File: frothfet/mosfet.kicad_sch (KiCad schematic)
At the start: 25 parts, among them Q1 AO3400A, Q2 BSC010N04LS, U1 SN74LVC1G14DBV, U2 LM74502H, U3 TMCS1108A2U

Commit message: bom and placement all check out.  ready for production!
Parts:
- Q2, U3: Rotation Offset (none) -> -90
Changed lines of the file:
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@@
+			)
+		)
+		(property "Rotation Offset" "-90"
+			(at 156.21 107.95 0)
+			(effects
+				(font
+					(size 1.27 1.27)
+				)
+				(hide yes)
 			)
 		)
@@
 			(at 143.51 58.42 0)
 			(effects
+				(font
+					(size 1.27 1.27)
+				)
+				(hide yes)
+			)
+		)
+		(property "Rotation Offset" "-90"
+			(at 143.51 58.42 0)
+			(effects

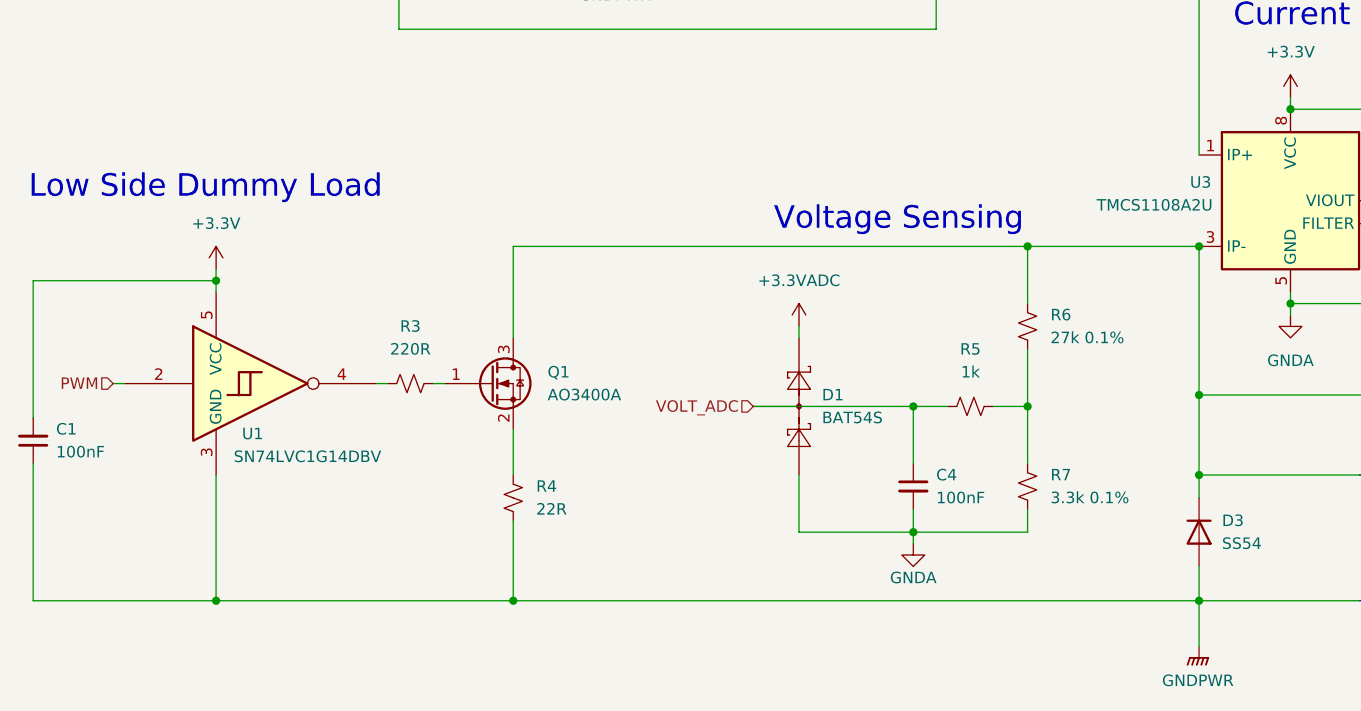
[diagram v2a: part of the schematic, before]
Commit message: removed unneccesary bleed circuit
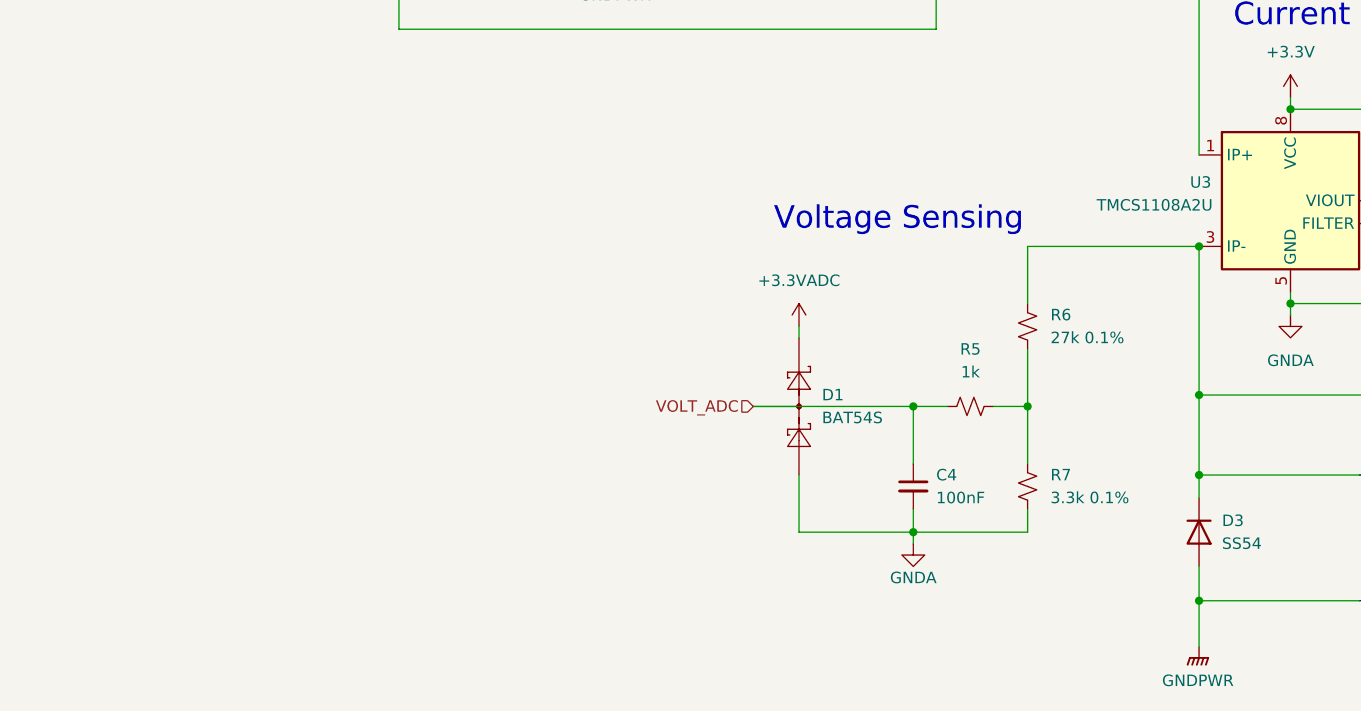
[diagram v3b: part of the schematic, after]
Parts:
- removed C1: 100nF, Capacitor_SMD:C_0603_1608Metric, symbol Device:C_Small
- removed Q1: AO3400A, Package_TO_SOT_SMD:SOT-23, symbol Transistor_FET:AO3400A
- removed R3: 220R, Resistor_SMD:R_0603_1608Metric, symbol Device:R_Small_US
- removed R4: 22R, Resistor_SMD:R_1206_3216Metric, symbol Device:R_Small_US
- removed U1: SN74LVC1G14DBV, Package_TO_SOT_SMD:SOT-23-5, symbol 74xGxx:SN74LVC1G14DBV
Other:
- note removed: "Low Side Dummy Load"

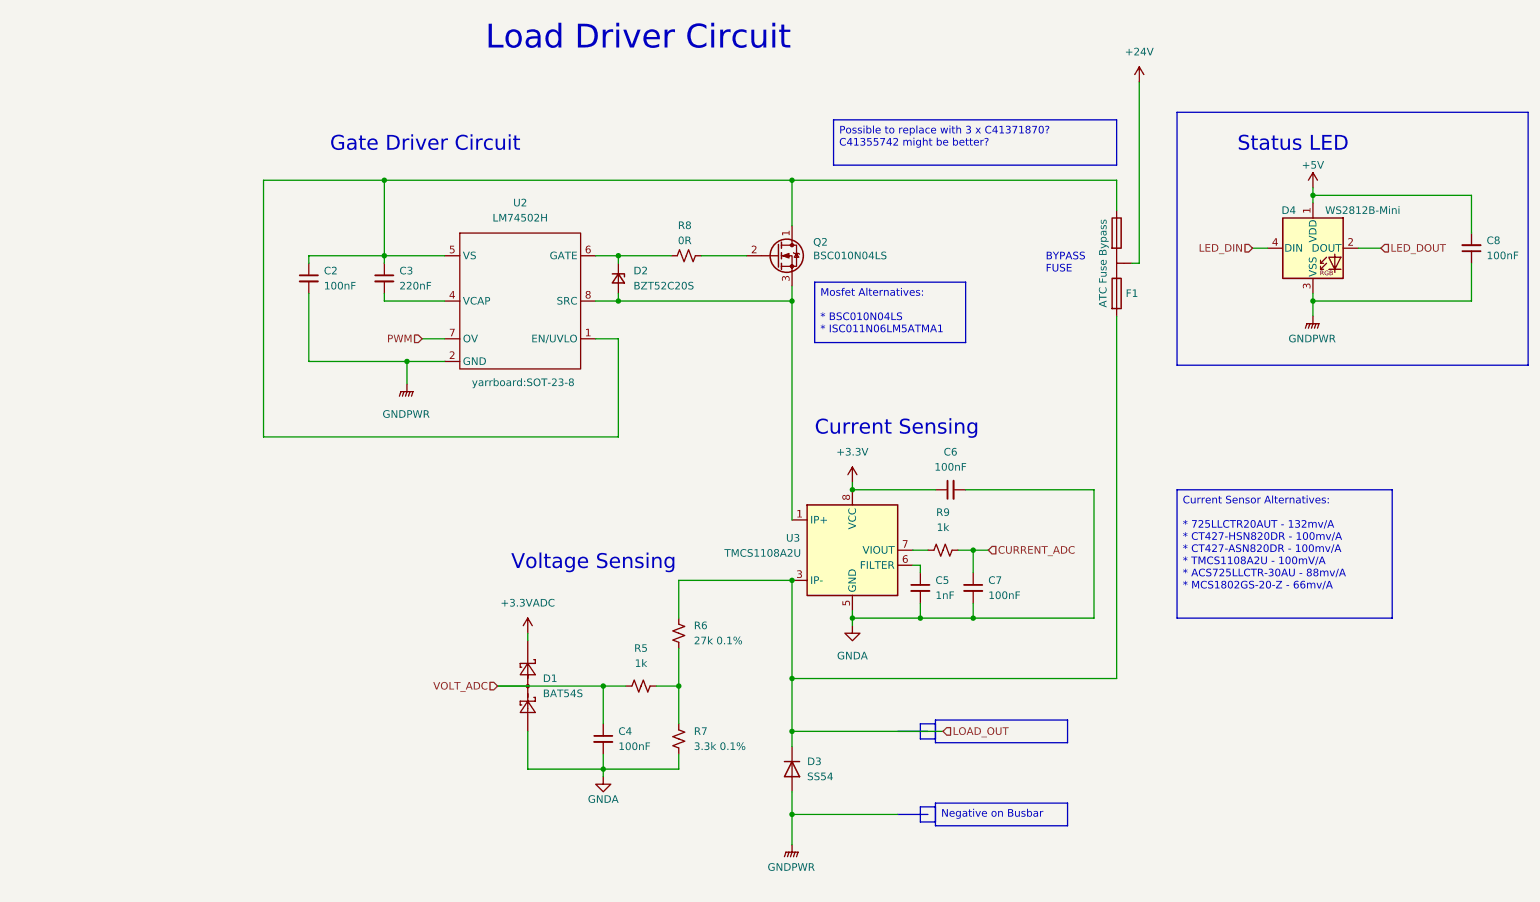
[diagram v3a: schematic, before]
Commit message: switched to ina226 for voltage and current measurement
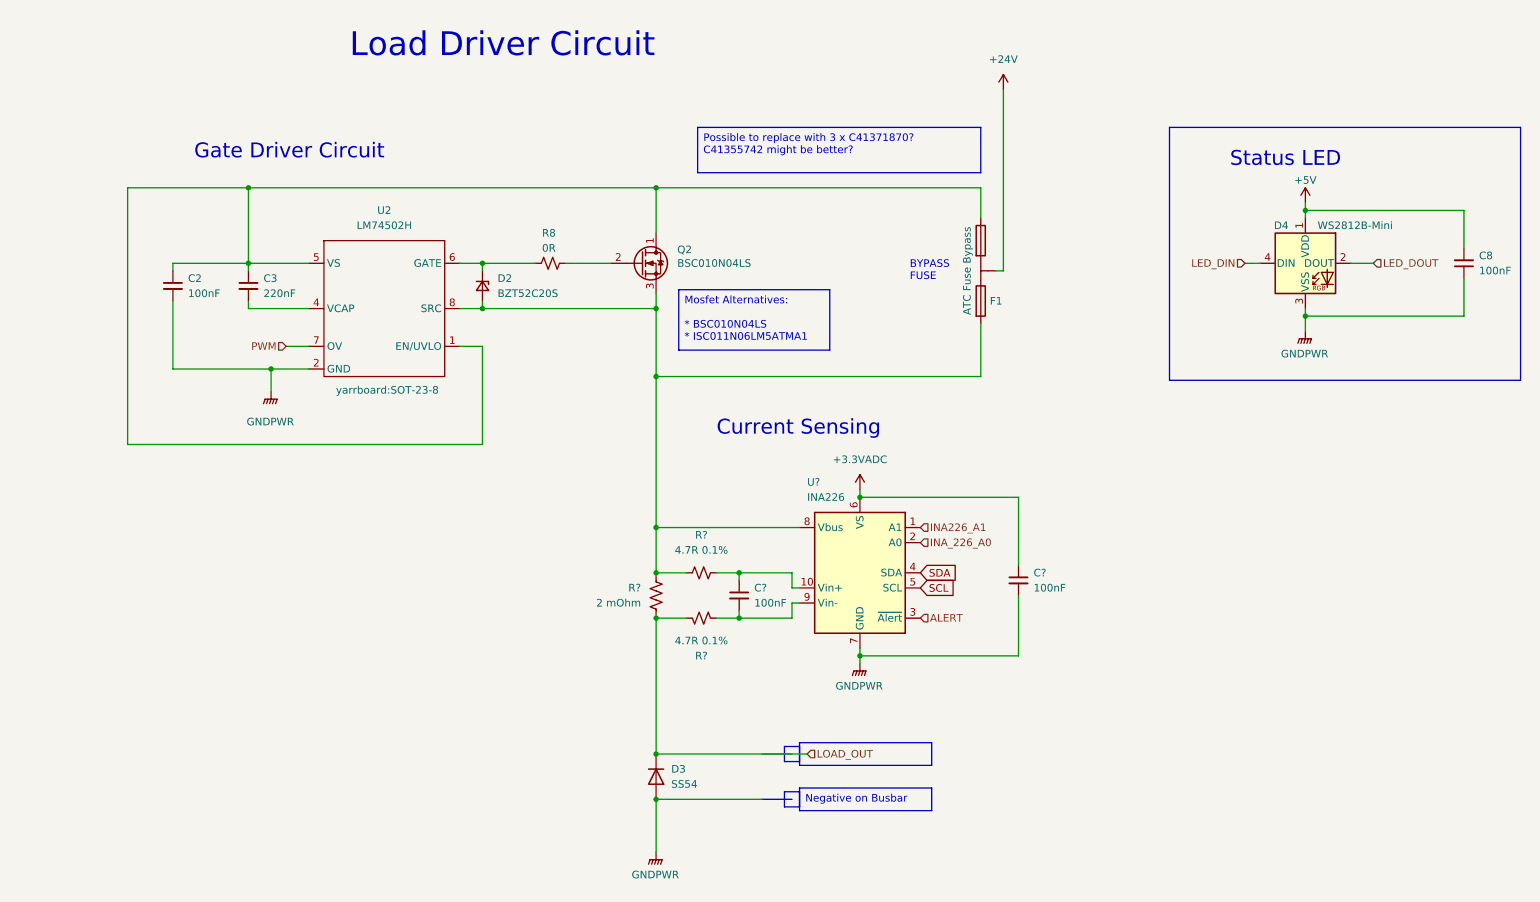
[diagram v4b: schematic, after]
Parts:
- removed C4, C6, C7: 100nF, Capacitor_SMD:C_0603_1608Metric, symbol Device:C_Small
- removed C5: 1nF, Capacitor_SMD:C_0603_1608Metric, symbol Device:C_Small
- removed D1: BAT54S, Package_TO_SOT_SMD:SOT-23, symbol Diode:BAT54S
- removed R5, R9: 1k, Resistor_SMD:R_0603_1608Metric, symbol Device:R_Small_US
- removed R6: 27k 0.1%, Resistor_SMD:R_0603_1608Metric, symbol Device:R_Small_US
- removed R7: 3.3k 0.1%, Resistor_SMD:R_0603_1608Metric, symbol Device:R_Small_US
- removed U3: TMCS1108A2U, yarrboard:ACS7XX, symbol Sensor_Current:ACS725xLCTR-20AU
- added C? (x2): 100nF, Capacitor_SMD:C_0603_1608Metric, symbol Device:C_Small
- added R?: 2 mOhm, Resistor_SMD:R_4020_10251Metric, symbol Device:R_US
- added R? (x2): 4.7R 0.1%, Resistor_SMD:R_0603_1608Metric, symbol Device:R_Small_US
- added U?: INA226, Package_SO:VSSOP-10_3x3mm_P0.5mm, symbol Sensor_Energy:INA226
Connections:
- net +3.3VADC: now also C?.1, U?.6 (VS)
- net GNDPWR: now also C?.2, U?.7 (GND)
- net LOAD_OUT: now also R?.2, R?.2; no longer F1.3
- net at D2.2 (A), Q2.3 (S), U2.8 (SRC): now also F1.3, R?.1, R?.2, U?.8 (Vbus)
- new net: C?.1, R?.1, U?.10 (Vin+)
- new net: C?.2, R?.1, U?.9 (Vin-)
- new net ALERT: U?.3 (~{Alert})
- new net INA226_A1: U?.1 (A1)
- new net INA_226_A0: U?.2 (A0)
- new net SCL: U?.5 (SCL)
- new net SDA: U?.4 (SDA)
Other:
- note removed: "Voltage Sensing"
- moved on the sheet: C2, C3, C8, D2, D3, D4, F1, Q2, R8, U2

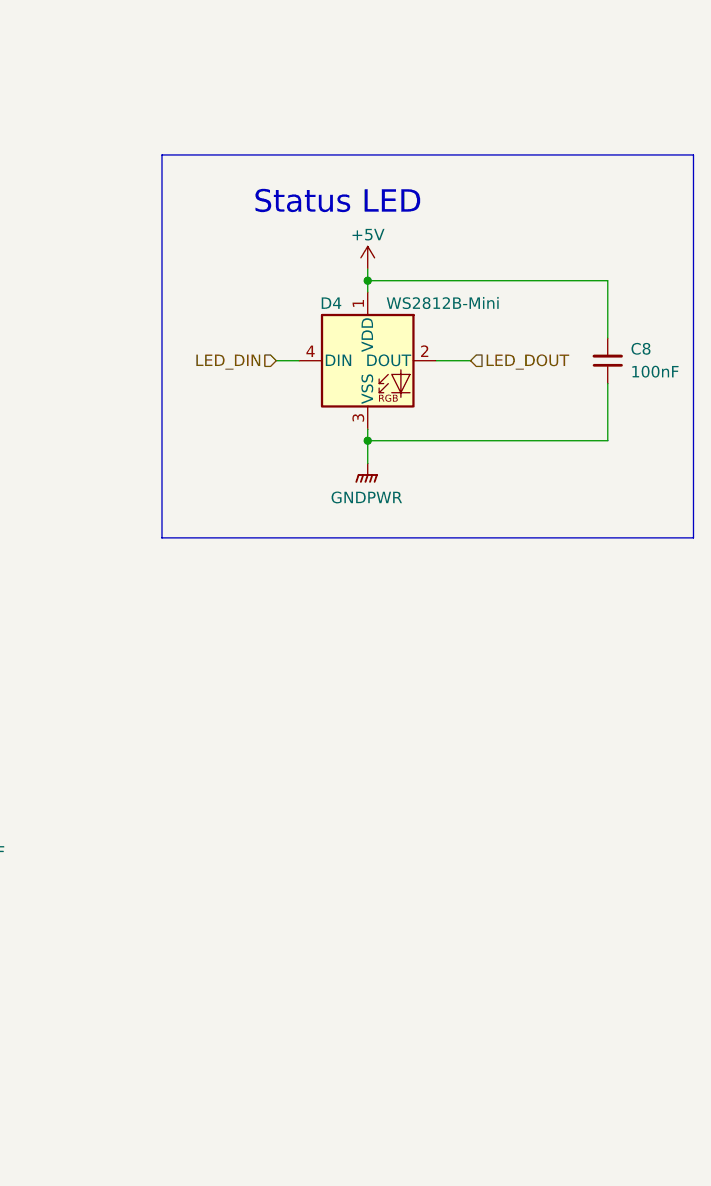
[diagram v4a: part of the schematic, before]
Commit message: added lm75b temperature sensor to channels.
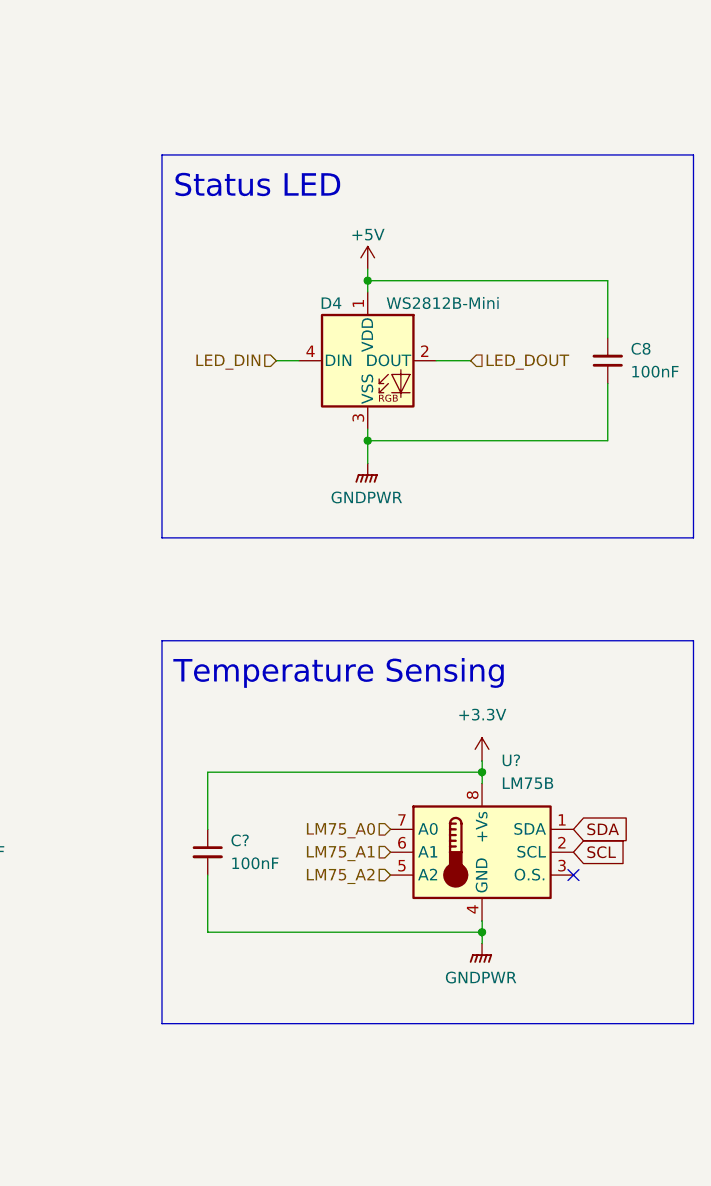
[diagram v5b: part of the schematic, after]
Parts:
- added C?: 100nF, Capacitor_SMD:C_0603_1608Metric, symbol Device:C_Small
- added U?: LM75B, symbol Sensor_Temperature:LM75B
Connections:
- net GNDPWR: now also C?.2, U?.4 (GND)
- net SCL: now also U?.2 (SCL)
- net SDA: now also U?.1 (SDA)
- new net +3.3V: C?.1, U?.8 (+Vs)
- new net LM75_A0: U?.7 (A0)
- new net LM75_A1: U?.6 (A1)
- new net LM75_A2: U?.5 (A2)
- no-connect marks 0 -> 1
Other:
- note added: "Temperature Sensing"

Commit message: wired the i2c addresses.
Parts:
- U3: renamed from U?; footprint (none) -> Package_SO:SOIC-8_3.9x4.9mm_P1.27mm; LCSC (none) -> C34565
- gave numbers to parts that had none: 7
- renumbered C2 to C1, C3 to C2, C8 to C6, D2 to D1, D3 to D2, D4 to D3, Q2 to Q1, R8 to R3, U2 to U1
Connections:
- net ALERT: no longer names the net of U2.3 (~{Alert})
- net INA_226_A0 renamed INA226_A0
- net LOAD_OUT renamed LOAD
- no-connect marks 1 -> 2

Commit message: added the buffer circuit
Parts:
- added R4: 10k, Resistor_SMD:R_0603_1608Metric, symbol Device:R_Small_US
- renumbered C1 to C2, C2 to C3, C3 to C4, C4 to C5, C5 to C6, C6 to C7, R3 to R5, R4 to R6, R5 to R7, R6 to R8, U1 to U2, U2 to U3, U3 to U4
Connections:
- net GNDPWR: now also R4.2
- net PWM: now also R4.1

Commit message: changed to a single ground
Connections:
- net +3.3V is gone; now on net +3.3VADC: C6.1, U4.8 (+Vs)
- net GNDPWR renamed GND
